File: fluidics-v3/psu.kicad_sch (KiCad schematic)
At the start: 11 parts, among them U3 AP7366EA-33W5-7, U4 D24V10FX

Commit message: U3: swap AP7366EA-33W5-7 -> AP2112K-3.3TRG1
Pin-compatible drop-in for the +3.3V LDO. Both parts are 600mA CMOS
LDOs with enable in SOT-23-5, and the fixed-output pin assignment is
identical (1=IN, 2=GND, 3=EN, 4=NC, 5=OUT), matching the board wiring
(+5V / GND / +5V / no-connect / +3.3V). Footprint unchanged
(Package_TO_SOT_SMD:SOT-23-5), so no layout impact.

Schematic, PCB and both BOMs updated together; schematic parity 0,
DRC 0 errors. Value text is on F.Fab only, so the existing gerbers and
positions.csv remain valid and were not regenerated.

Note: order the FIXED 3.3V variant. On the ADJ version pin 4 is the
feedback pin, not a no-connect.

Co-Authored-By: Claude Opus 5 (1M context) <noreply@anthropic.com>
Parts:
- U3: value AP7366EA-33W5-7 -> AP2112K-3.3TRG1
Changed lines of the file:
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@@
 			)
 		)
-		(property "Value" "AP7366EA-33W5-7"
+		(property "Value" "AP2112K-3.3TRG1"
 			(at 27.94 45.72 0)
 			(show_name no)

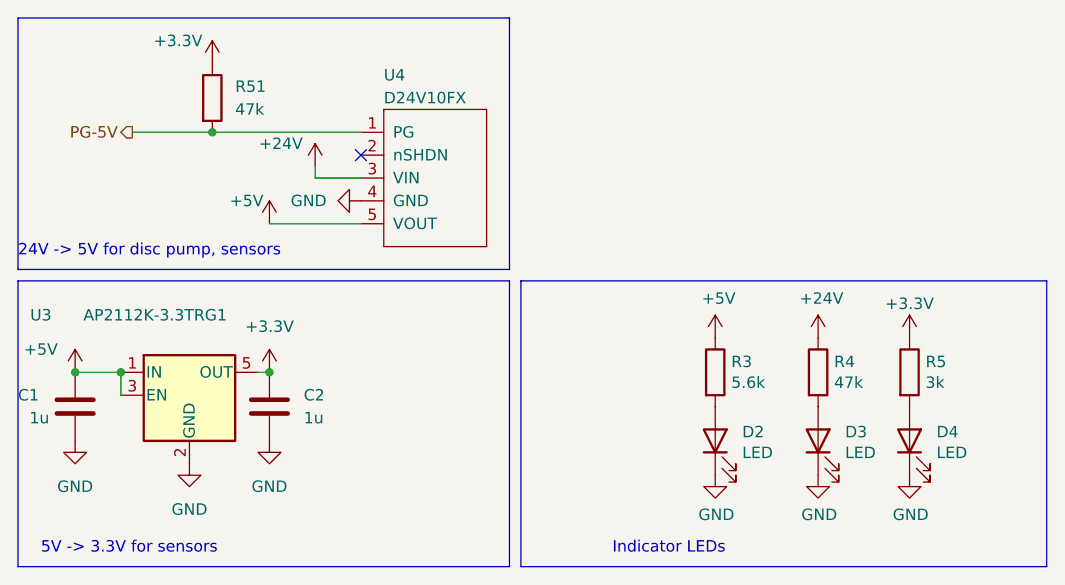
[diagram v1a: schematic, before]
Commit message: U4: replace Pololu D24V10FX with Traco TSR1-2450E, drop 5V power-good
Swap the 24V->5V step-down for a Traco TSR 1-2450E (SIP-3, through-hole,
1A) using the stock KiCad symbol/footprint pair. The TSR is a 3-pin part,
so the Pololu's PG and nSHDN pins go away; nSHDN was already unconnected.

Schematic:
- psu: U4 -> Converter_DCDC:TSR1-2450E on
  Converter_DCDC:Converter_DCDC_TRACO_TSR1-xxxxE_THT
- Remove the PG-5V hierarchical label, sheet pin, wire stub and the 47k
  pull-up R51; PG-5V no longer exists as a net
- No-connect flags on J7 pin 1 and U2 pin 25, freeing Teensy pin 33

PCB:
- Place U4 at (156.437, 71.905) rot +90 so Vin lands on the existing +24V
  arrival node; GND and Vout follow on the 2.54mm pitch. Rotating rather
  than mirroring keeps the TSR body clear of R3 and D2, which the part
  would otherwise sit on top of.
- Route +5V on F.Cu 0.55mm from the existing tap across to Vout, plus a
  via restoring the F.Cu/B.Cu junction the old through-hole pad provided
- Remove orphaned PG-5V copper (16 segments, 2 vias) and the now-dead
  6-segment +3.3V run that used to feed R51

DRC: 0 errors, schematic parity clean, unconnected 7 -> 6.
Courtyard overlaps 2 -> 0, dangling tracks 4 -> 0. ERC 33 -> 31.
One cosmetic silkscreen warning remains: the "24V->5V Module" board label
now overlaps U4's outline and wants nudging by hand.

Co-Authored-By: Claude Opus 5 (1M context) <noreply@anthropic.com>
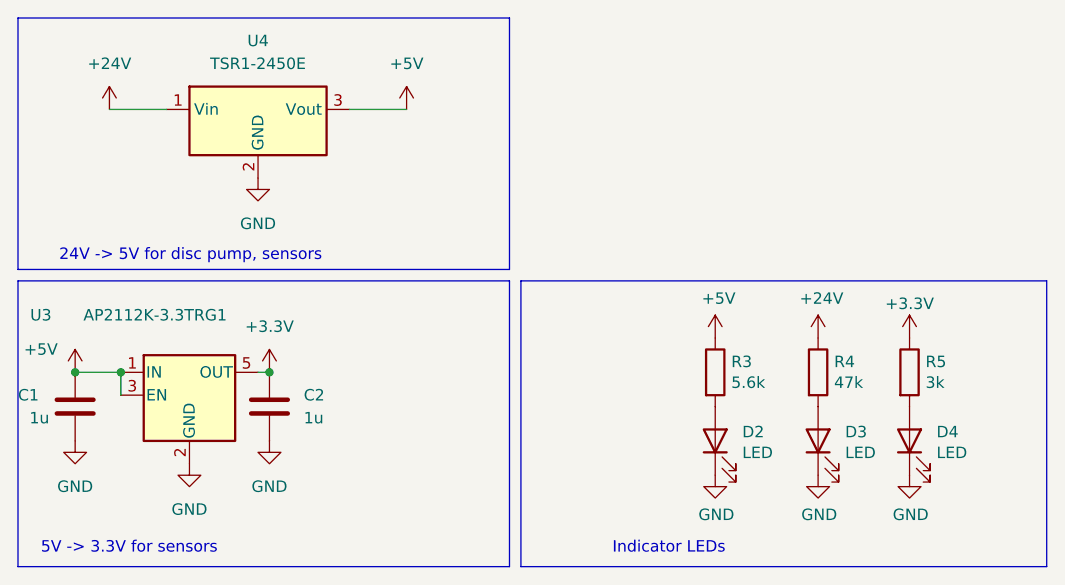
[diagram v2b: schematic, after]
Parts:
- removed R51: 47k, Resistor_SMD:R_0603_1608Metric_Pad0.98x0.95mm_HandSolder, symbol Device:R
- removed U4: D24V10FX, pololu:D24V10FX, symbol pololu:D24V10FX
- added U4: TSR1-2450E, Converter_DCDC:Converter_DCDC_TRACO_TSR1-xxxxE_THT, symbol Converter_DCDC:TSR1-2450E
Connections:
- net +24V: now also U4.1 (Vin)
- net +5V: now also U4.3 (Vout)
- net GND: now also U4.2 (GND)
- no-connect marks 1 -> 0

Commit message: v3: +24V soft-start front end, U1 COM bypass, silkscreen and BOM fixes
Power input stage
- Replace TH1 (10 ohm NTC) with a low-side N-channel soft-start: Q1 (F60N80,
  TO-220) with a 100k/68k gate divider (R2/R6) and 0.1u timing cap (C11).
  The NTC sat in series with the whole board and dissipated 1.5-10 W; at
  1.85 A it was already over a 7 mm disc's rating before any valve moved.
- Split ground: /GND1 (J1 shell + pin 2) is now separate from GND, with Q1
  bridging them. Removed a leftover 2.39 mm GND track that still touched
  J1.S2 and shorted straight across Q1.
- Add C12 470u/50V bulk and C13 0.1u HF bypass on +24V. C3 alone left the
  300 kHz - 100 MHz band uncovered while U4 switches at 500 kHz.
- Route the block: gate net kept inside 5 mm of Q1's gate; /GND1 return at
  1.50 mm (4.3 A capacity vs 1.85 A worst case through Q1).

Solenoid driver
- Add C25 0.1u across U1 pin 9 (COM) to GND. That node catches flyback from
  all seven channels and previously reached the +24V plane through ~50 mm of
  0.55 mm trace with nothing local.

Silkscreen
- Raise 403 graphic objects from 0.000/0.100/0.120/0.127 mm to the 0.15 mm
  fab minimum; five were zero-width, which is undefined behaviour. Fix one
  0.45 mm text height and one 0.09 mm stroke.
- Selector valve legend: label 'J23' named a part that does not exist; the
  connector there is J25. Recentre all 12 labels on their own connectors,
  strip stray newlines, and hide 7 duplicate footprint refdes that sat
  midway between connectors and read as shifted by one.

Cleanup
- Remove two /SDA and /SCL vias that connected B.Cu to B.Cu after those nets
  moved to the back layer, and split a +3.3V track so its end meets a
  junction rather than landing mid-span.
- Stitch an orphaned F.Cu ground island that had captured D3's cathode pad.

BOM
- Correct three MPNs that contradicted their own values and packages:
  R3 5.6k/0805 was a 680R 0603 part, R4 47k/0402 was a 4k7 0603 part,
  R5 3k/0402 was a 270R 0603 part.
- J1 car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
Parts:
- R3: Manufacturer_Part_Number RT0603DRD07680RL -> RC0805FR-075K6L
- R4: Manufacturer_Part_Number RC0603FR-074K7L -> RC0402FR-0747KL
- R5: Manufacturer_Part_Number RC0603FR-07270RL -> RC0402FR-073KL
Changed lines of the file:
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@@
+	)
+	(junction
+		(at 22.86 22.86)
+		(diameter 0)
+		(color 0 0 0 0)
 	)
 	(junction
@@
 		)
 		(instances
-			(project "fluidics-v2"
+			(project "fluidics-v3"
 				(path "/0ec91c42-8aad-437d-8c85-5e10f0e51fe0/3165fef8-6560-4a32-9d6f-43437086a53c"
 					(reference "#PWR062")
@@
 		)
 		(instances
-			(project "fluidics-v2"
+			(project "fluidics-v3"
 				(path "/0ec91c42-8aad-437d-8c85-5e10f0e51fe0/3165fef8-6560-4a32-9d6f-43437086a53c"
 					(reference "#PWR060")
@@
 		)
 		(instances
-			(project "fluidics-v2"
+			(project "fluidics-v3"
 				(path "/0ec91c42-8aad-437d-8c85-5e10f0e51fe0/3165fef8-6560-4a32-9d6f-43437086a53c"
 					(reference "D2")
@@
 		)
 		(instances
-			(project "fluidics-v2"
+			(project "fluidics-v3"
 				(path "/0ec91c42-8aad-437d-8c85-5e10f0e51fe0/3165fef8-6560-4a32-9d6f-43437086a53c"
 					(reference "#PWR061")
+					(unit 1)
+				)
+			)
+		)
+	)
+	(symbol
+		(lib_id "power:PWR_FLAG")
+		(at 22.86 22.86 180)
+		(unit 1)
+		(body_style 1)
+		(exclude_from_sim no)
+		(in_bom yes)
+		(on_board yes)
+		(in_pos_files yes)
+		(dnp no)
+		(fields_autoplaced yes)
+		(property "Reference" "#FLG03"
+			(at 22.86 24.765 0)
+			(hide yes)
+			(show_name no)
+			(do_not_autoplace no)
+			(effects
+				(font
+					(size 1.27 1.27)
+				)
+			)
+		)
+		(property "Value" "PWR_FLAG"
+			(at 22.86 27.94 0)
+			(show_name no)
+			(do_not_autoplace no)
+			(effects
+				(font
+					(size 1.27 1.27)
+				)
+			)
+		)
+		(property "Footprint" ""
+			(at 22.86 22.86 0)
+			(hide yes)
+			(show_name no)
+			(do_not_autoplace no)
+			(effects
+				(font
+					(size 1.27 1.27)
+				)
+			)
+		)
+		(property "Datasheet" ""
+			(at 22.86 22.86 0)
+			(hide yes)
+			(show_name no)
+			(do_not_autoplace no)
+			(effects
+				(font
+					(size 1.27 1.27)
+				)
+			)
+		)
+		(property "Description" "Special symbol for telling ERC where power comes from"
+			(at 22.86 22.86 0)
+			(hide yes)
+			(show_name no)
+			(do_not_autoplace no)
+			(effects
+				(font
+					(size 1.27 1.27)
+				)
+			)
+		)
+		(pin "1"
+		)
+		(instances
+			(project "fluidics-v3"
+				(path "/0ec91c42-8aad-437d-8c85-5e10f0e51fe0/3165fef8-6560-4a32-9d6f-43437086a53c"
+					(reference "#FLG03")
 					(unit 1)
 				)
@@
 		)
 		(instances
-			(project "fluidics-v2"
+			(project "fluidics-v3"
 				(path "/0ec91c42-8aad-437d-8c85-5e10f0e51fe0/3165fef8-6560-4a32-9d6f-43437086a53c"
 					(reference "D3")
@@
 		)
 		(instances
-			(project "fluidics-v2"
+			(project "fluidics-v3"
 				(path "/0ec91c42-8aad-437d-8c85-5e10f0e51fe0/3165fef8-6560-4a32-9d6f-43437086a53c"
 					(reference "#PWR06")
@@
 		)
 		(instances
-			(project "fluidics-v2"
+			(project "fluidics-v3"
 				(path "/0ec91c42-8aad-437d-8c85-5e10f0e51fe0/3165fef8-6560-4a32-9d6f-43437086a53c"
 					(reference "#PWR065")
@@
 		)
 		(instances
-			(project "fluidics-v2"
+			(project "fluidics-v3"
 				(path "/0ec91c42-8aad-437d-8c85-5e10f0e51fe0/3165fef8-6560-4a32-9d6f-43437086a53c"
 					(reference "C2")
@@
 		)
 		(instances
-			(project "fluidics-v2"
+			(project "fluidics-v3"
 				(path "/0ec91c42-8aad-437d-8c85-5e10f0e51fe0/3165fef8-6560-4a32-9d6f-43437086a53c"
 					(reference "#PWR067")
@@
 			)
 		)
-		(property "Manufacturer_Part_Number" "RT0603DRD07680RL"
+		(property "Manufacturer_Part_Number" "RC0805FR-075K6L"
 			(at 90.17 52.07 0)
 			(hide yes)
@@
 		)
 		(instances
-			(project "fluidics-v2"
+			(project "fluidics-v3"
 				(path "/0ec91c42-8aad-437d-8c85-5e10f0e51fe0/3165fef8-6560-4a32-9d6f-43437086a53c"
 					(reference "R3")
@@
 		)
 		(instances
-			(project "fluidics-v2"
+			(project "fluidics-v3"
 				(path "/0ec91c42-8aad-437d-8c85-5e10f0e51fe0/3165fef8-6560-4a32-9d6f-43437086a53c"
 					(reference "C1")
@@
 		)
 		(instances
-			(project "fluidics-v2"
+			(project "fluidics-v3"
 				(path "/0ec91c42-8aad-437d-8c85-5e10f0e51fe0/3165fef8-6560-4a32-9d6f-43437086a53c"
 					(reference "U4")
@@
 		)
 		(instances
-			(project "fluidics-v2"
+			(project "fluidics-v3"
 				(path "/0ec91c42-8aad-437d-8c85-5e10f0e51fe0/3165fef8-6560-4a32-9d6f-43437086a53c"
 					(reference "#PWR066")
@@
 		)
 		(instances
-			(project "fluidics-v2"
+			(project "fluidics-v3"
 				(path "/0ec91c42-8aad-437d-8c85-5e10f0e51fe0/3165fef8-6560-4a32-9d6f-43437086a53c"
 					(reference "#PWR076")
@@
 		)
 		(instances
-			(project "fluidics-v2"
+			(project "fluidics-v3"
 				(path "/0ec91c42-8aad-437d-8c85-5e10f0e51fe0/3165fef8-6560-4a32-9d6f-43437086a53c"
 					(reference "#PWR077")
@@
 			)
 		)
-		(property "Manufacturer_Part_Number" "RC0603FR-074K7L"
+		(property "Manufacturer_Part_Number" "RC0402FR-0747KL"
 			(at 101.6 52.07 0)
 			(hide yes)
@@
 		)
 		(instances
-			(project "fluidics-v2"
+			(project "fluidics-v3"
 				(path "/0ec91c42-8aad-437d-8c85-5e10f0e51fe0/3165fef8-6560-4a32-9d6f-43437086a53c"
 					(reference "R4")
@@
 		)
 		(instances
-			(project "fluidics-v2"
+			(project "fluidics-v3"
 				(path "/0ec91c42-8aad-437d-8c85-5e10f0e51fe0/3165fef8-6560-4a32-9d6f-43437086a53c"
 					(reference "#PWR021")
@@
 		)
 		(instances
-			(project "fluidics-v2"
+			(project "fluidics-v3"
 				(path "/0ec91c42-8aad-437d-8c85-5e10f0e51fe0/3165fef8-6560-4a32-9d6f-43437086a53c"
 					(reference "#PWR079")
@@
 		)
 		(instances
-			(project "fluidics-v2"
+			(project "fluidics-v3"
 				(path "/0ec91c42-8aad-437d-8c85-5e10f0e51fe0/3165fef8-6560-4a32-9d6f-43437086a53c"
 					(reference "U3")
@@
 		)
 		(instances
-			(project "fluidics-v2"
+			(project "fluidics-v3"
 				(path "/0ec91c42-8aad-437d-8c85-5e10f0e51fe0/3165fef8-6560-4a32-9d6f-43437086a53c"
 					(reference "#PWR073")
@@
 		)
 		(instances
-			(project "fluidics-v2"
+			(project "fluidics-v3"
 				(path "/0ec91c42-8aad-437d-8c85-5e10f0e51fe0/3165fef8-6560-4a32-9d6f-43437086a53c"
 					(reference "D4")
@@
 		)
 		(instances
-			(project "fluidics-v2"
+			(project "fluidics-v3"
 				(path "/0ec91c42-8aad-437d-8c85-5e10f0e51fe0/3165fef8-6560-4a32-9d6f-43437086a53c"
 					(reference "#PWR072")
@@
 		)
 		(instances
-			(project "fluidics-v2"
+			(project "fluidics-v3"
 				(path "/0ec91c42-8aad-437d-8c85-5e10f0e51fe0/3165fef8-6560-4a32-9d6f-43437086a53c"
 					(reference "#PWR078")
@@
 			)
 		)
-		(property "Manufacturer_Part_Number" "RC0603FR-07270RL"
+		(property "Manufacturer_Part_Number" "RC0402FR-073KL"
 			(at 111.76 52.07 0)
 			(hide yes)
@@
 		)
 		(instances
-			(project "fluidics-v2"
+			(project "fluidics-v3"
 				(path "/0ec91c42-8aad-437d-8c85-5e10f0e51fe0/3165fef8-6560-4a32-9d6f-43437086a53c"
 					(reference "R5")

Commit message: fab: apply JLCPCB part selections to BOM, annotate strays, normalise CPL
Sourcing
- Write Manufacturer_Part_Number / Manufacturer_Name / LCSC for every part
  from the JLCPCB BOM-matching sheet. 33 of 34 BOM rows now carry an LCSC
  code; the exception is J10/J12/J14/J18/J21/J25 (Molex 87832-0410), which
  JLCPCB returned "No matches" for and still needs a part chosen.

Substitutions accepted from the sheet
- IC2  ADuM1250WSRZ-RL7 -> ISO1640BDR (TI). Verified pin-for-pin against the
  board: 1 VCC1, 2 SDA1, 3 SCL1, 4 GND1, 5 GND2, 6 SCL2, 7 SDA2, 8 VCC2.
- C3   -> KEMET T521X336M050ATE050, which is 33uF/50V, not 100uF. Value
  updated to match. The 50 V rating fixes the derating problem the old
  unrated 100uF tantalum had on a 24 V rail; 33uF is ample now that C12
  carries 470uF ten millimetres away. Note the part is case X (7343-43,
  4.3 mm tall) against a footprint named 7343-20 - the land pattern is
  identical, only the height differs, and nothing sits above it.
- Q1   -> IRF540NPBF, J3 -> Connfly DS1037, D4 -> KT-0805R, J5 -> XY308.
- U13's MPN arrived truncated from JLCPCB as "TC7PZ17FU,LJ(CT"; restored the
  closing parenthesis.

Annotation
- D2/D3/D4, R3/R4/R5 (psu sheet) and H2/H3/H4 (root) were still unannotated
  "D?"/"R?"/"H?" symbols, so the BOM exporter was auto-numbering them on each
  run and no field edit could reach them. Annotated from the PCB footprint
  UUID paths rather than by position - H3 and H4 turned out to be the reverse
  of what their schematic coordinates suggested.

CPL
- Rotations now emitted 0-360; KiCad wrote 27 of them as negative (-90).
- Coordinates to 4 dp, rotation to 2 dp.
- BOM and CPL reconcile at 76 designators, no ranges, nothing one-sided.

ERC: 0 errors.

Co-Authored-By: Claude Opus 5 (1M context) <noreply@anthropic.com>
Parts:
- C1, C2: LCSC (none) -> C15849; Manufacturer_Name (none) -> Samsung Electro-Mechanics; Manufacturer_Part_Number (none) -> CL10A105KB8NNNC
- D2, D3: LCSC (none) -> C364562; Manufacturer_Name (none) -> Lite-On
- D4: LCSC (none) -> C2295; Manufacturer_Name (none) -> Hubei KENTO Elec; Manufacturer_Part_Number EAST2012WA1 -> KT-0805R
- R3: LCSC (none) -> C4382; Manufacturer_Name (none) -> UNI-ROYAL(Uniroyal Elec); Manufacturer_Part_Number RC0805FR-075K6L -> 0805W8F5601T5E
- R4: LCSC (none) -> C25792; Manufacturer_Name (none) -> UNI-ROYAL(Uniroyal Elec); Manufacturer_Part_Number RC0402FR-0747KL -> 0402WGF4702TCE
- R5: LCSC (none) -> C140159; Manufacturer_Name (none) -> FH (Guangdong Fenghua Advanced Tech); Manufacturer_Part_Number RC0402FR-073KL -> RC-02K3001FT
- U3: LCSC (none) -> C23380830; Manufacturer_Name (none) -> TECH PUBLIC; Manufacturer_Part_Number (none) -> AP2112K-3.3TRG1
- U4: LCSC (none) -> C5346721; Manufacturer_Name (none) -> TRACO POWER; Manufacturer_Part_Number (none) -> TSR 1-2450E
